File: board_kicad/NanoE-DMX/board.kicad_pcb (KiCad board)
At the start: 2 copper layers, 68.6 x 53.3 mm, 54 parts, among them J1 Conn_01x02, J20 Conn_01x02, J30 Conn_01x03, J40 RJ45, Q20 IRLM5203 (PMOS_GSD), Q21 IRLM5203 (PMOS_GSD), U1 Arduino_Nano_Every, U2 74LVC2G34, U20 TPS259630, U30 ADUM1301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

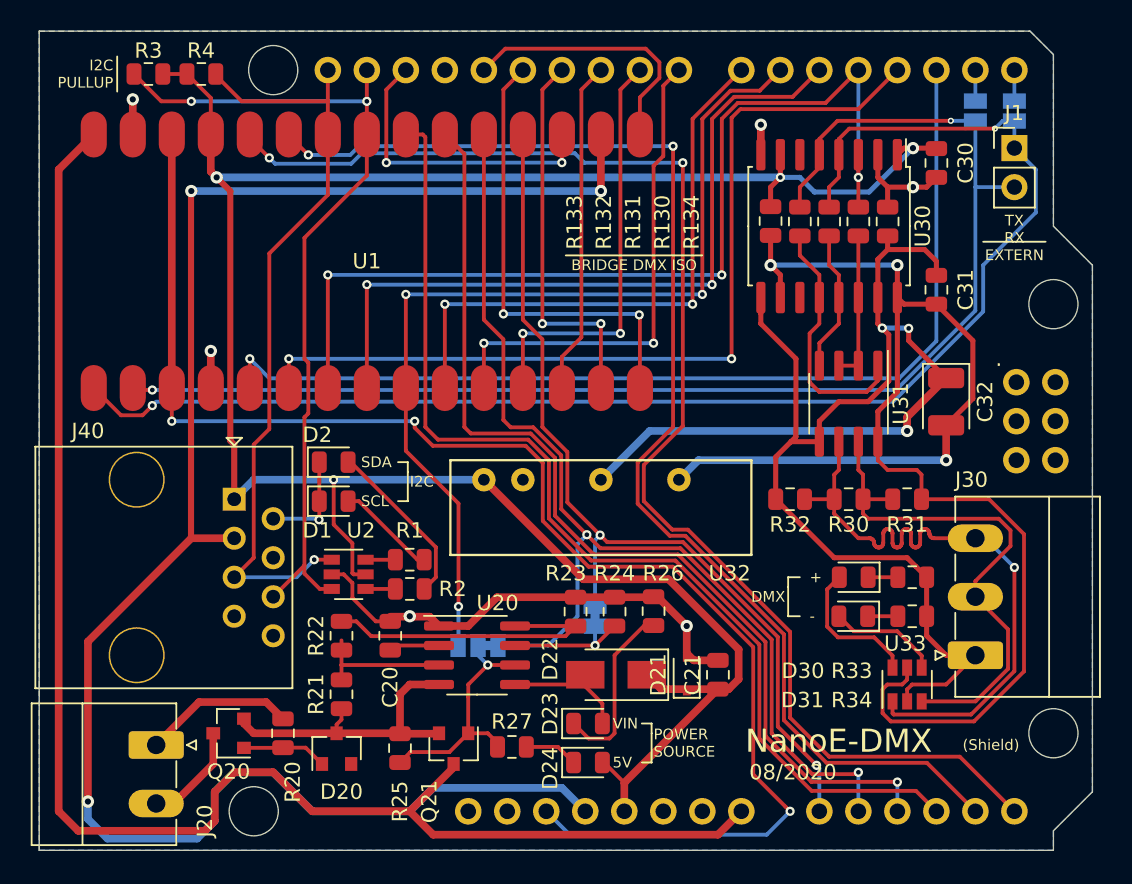
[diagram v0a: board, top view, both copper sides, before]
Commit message: added values and manufacurer id (kicost), improvements
BOTH
- added missing values for resitors and diodes
- added manf# for calculating and ordering with kicost
- minor improvements

NanoE-dmx
- bus controll LEDs (buffered) fixed for TX/RX, SDA/SCL
- changed J40 (RJ45(8pol)->Conn(4pol)
- added ISO 5V LED

UI-Shield
- Replaced U2 (MAX5026->LM2705), for higher max current
- added 2 leds at NC IO ports
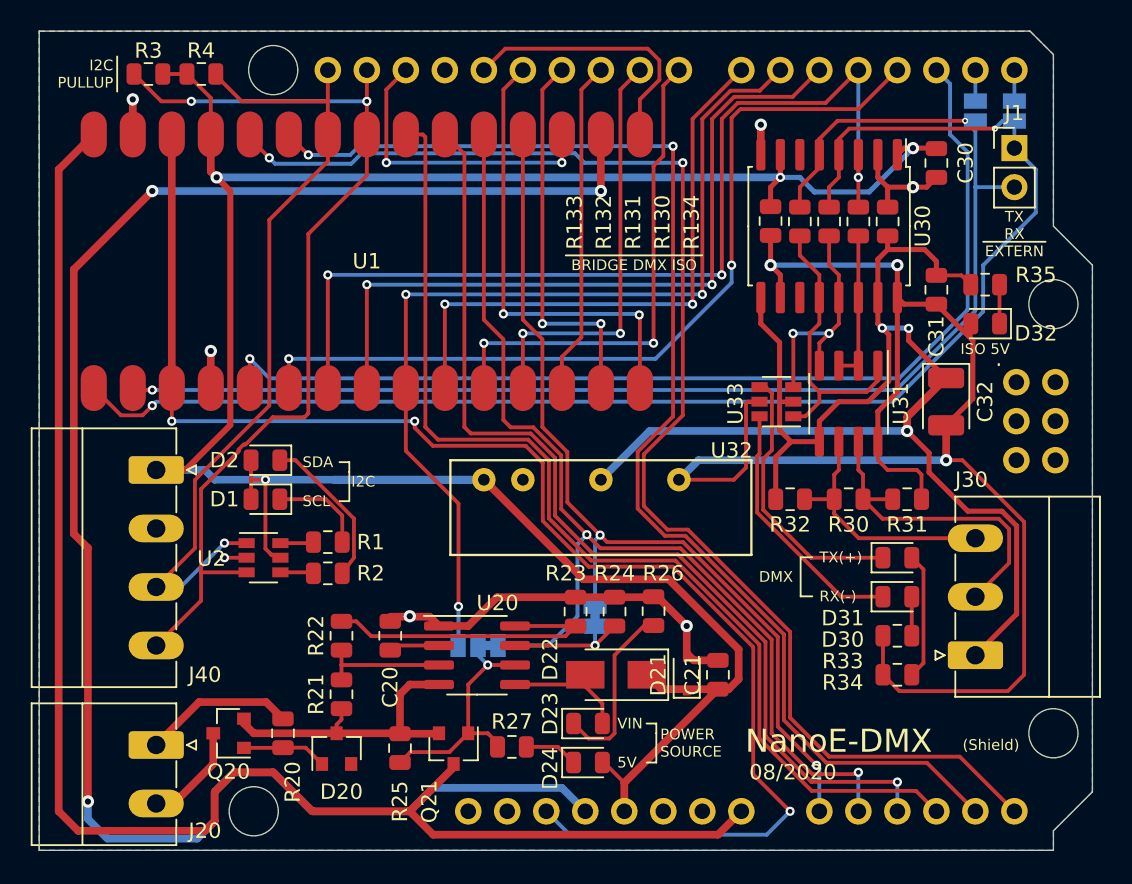
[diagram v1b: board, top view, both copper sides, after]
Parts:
- added D32: LED red, LED_SMD:LED_0805_2012Metric, F.Cu at (153.0, 95.2)
- added R35: 560, Resistor_SMD:R_0805_2012Metric, F.Cu at (153.0, 92.7)
- D1, D2, D30, D31: value LED -> LED yellow
- D23: value LED -> LED orange
- D24: value LED -> LED green
- J40: value RJ45 -> Conn_01x04; footprint Connector_RJ:RJ45_OST_PJ012-8P8CX_Vertical -> Connector_Phoenix_MC:PhoenixContact_MC_1,5_4-G-3.81_1x04_P3.81mm_Horizontal
- R1, R2, R26, R27, R33, R34: value 270 -> 560
- U32: value DCDC-SIP7-1-2-4-6 -> RFB-0505S
- moved U33 20.3 mm to (139.4, 100.3), turned to 180 degrees
- moved U2 5.65 mm to (106.0, 110.5)
- moved R1 5.46 mm to (110.2, 109.5)
- moved R2 5.43 mm to (110.2, 111.5)
- moved J40 5.43 mm to (99.1, 104.8)
- moved D31 4.77 mm to (147.3, 110.5), turned to 0 degrees
- moved D1 4.45 mm to (106.2, 106.7), turned to 180 degrees
- moved D2 4.45 mm to (106.2, 104.1), turned to 180 degrees
- moved R34 3.93 mm to (147.3, 118.1), turned to 0 degrees
- moved R33 3.93 mm to (147.3, 115.6), turned to 0 degrees
- moved D30 3.11 mm to (147.3, 113.0), turned to 0 degrees
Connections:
- D1 pad 1: GND -> Net-(D1-Pad1)
- D1 pad 2: Net-(D1-Pad2) -> +5V
- D2 pad 1: GND -> Net-(D2-Pad1)
- D2 pad 2: Net-(D2-Pad2) -> +5V
- J40 pad 3: +3V3 -> /SCL
- J40 pad 4: /IO3 -> /SDA
- R1 pad 1: Net-(D1-Pad2) -> Net-(D1-Pad1)
- R2 pad 1: Net-(D2-Pad2) -> Net-(D2-Pad1)
- R33 pad 1: /ISO_GND -> /ISO_+5V
- R33 pad 2: Net-(D30-Pad1) -> Net-(D30-Pad2)
- R34 pad 1: /ISO_GND -> /ISO_+5V
- R34 pad 2: Net-(D31-Pad1) -> Net-(D31-Pad2)
- U33 pad 1: /DMX+ -> /ISO_RX
- U33 pad 3: /DMX- -> /ISO_TX
- U33 pad 4: Net-(D31-Pad2) -> Net-(D31-Pad1)
- U33 pad 6: Net-(D30-Pad2) -> Net-(D30-Pad1)
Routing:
- net /DMX+: track 42.1 -> 17.2 mm, vias 1 -> 0
- net +5V: track 150.2 -> 167.6 mm
- net Net-(D31-Pad1): track 1.97 -> 17.9 mm
- net Net-(D30-Pad1): track 1.94 -> 16.8 mm
- net /DMX-: track 34.1 -> 21.4 mm
- net GND: track 61.2 -> 50.2 mm
- net Net-(D2-Pad2): track 10.9 -> 0.00 mm
- net Net-(D2-Pad1): track 0.00 -> 10.2 mm
- net /ISO_+5V: track 96.5 -> 105.3 mm
- net /SDA: track 55.6 -> 63.3 mm
- net Net-(D30-Pad2): track 9.36 -> 2.54 mm
- net Net-(D1-Pad2): track 6.36 -> 0.00 mm
- net Net-(D1-Pad1): track 0.00 -> 6.23 mm
- net /ISO_TX: track 9.24 -> 15.1 mm, vias 0 -> 2
- net /SCL: track 50.4 -> 53.4 mm
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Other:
- board text added: "ISO 5V"
- board text added: "RX(-)"
- board text added: "TX(+)"
- board text removed: "+"
- board text removed: "-"

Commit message: minor cleanup
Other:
- board text added: "RX"
- board text added: "TX"
- board text removed: "RX(-)"
- board text removed: "TX(+)"
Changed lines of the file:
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@@
     (effects (font (size 0.7 0.7) (thickness 0.1)) (justify right))
   )
-  (gr_line (start 141.0208 113.0046) (end 141.0208 110.49) (layer F.SilkS) (width 0.12))
-  (gr_text "RX(-)" (at 142.24 113.0046) (layer F.SilkS)
-    (effects (font (size 0.7 0.7) (thickness 0.1)) (justify left))
-  )
-  (gr_text DMX (at 138.303 111.7346) (layer F.SilkS)
-    (effects (font (size 0.7 0.7) (thickness 0.1)) (justify left))
-  )
-  (gr_line (start 141.7828 113.0046) (end 141.0208 113.0046) (layer F.SilkS) (width 0.12))
-  (gr_text "TX(+)" (at 142.24 110.4646) (layer F.SilkS)
-    (effects (font (size 0.7 0.7) (thickness 0.1)) (justify left))
-  )
-  (gr_line (start 141.7828 110.4646) (end 141.0208 110.4646) (layer F.SilkS) (width 0.12))
+  (gr_line (start 142.1003 113.0046) (end 142.1003 110.49) (layer F.SilkS) (width 0.12))
+  (gr_text RX (at 143.3195 113.0046) (layer F.SilkS)
+    (effects (font (size 0.7 0.7) (thickness 0.1)) (justify left))
+  )
+  (gr_text DMX (at 139.3825 111.7346) (layer F.SilkS)
+    (effects (font (size 0.7 0.7) (thickness 0.1)) (justify left))
+  )
+  (gr_line (start 142.8623 113.0046) (end 142.1003 113.0046) (layer F.SilkS) (width 0.12))
+  (gr_text TX (at 143.3195 110.4646) (layer F.SilkS)
+    (effects (font (size 0.7 0.7) (thickness 0.1)) (justify left))
+  )
+  (gr_line (start 142.8623 110.4646) (end 142.1003 110.4646) (layer F.SilkS) (width 0.12))
   (gr_line (start 110.998 106.807) (end 111.633 106.807) (layer F.SilkS) (width 0.12))
   (gr_line (start 110.998 104.267) (end 111.633 104.267) (layer F.SilkS) (width 0.12))
@@
   (segment (start 98.806 99.568) (end 147.236276 99.568) (width 0.25) (layer B.Cu) (net 24))
   (segment (start 154.94 86.36) (end 152.4 86.36) (width 0.25) (layer B.Cu) (net 24) (status 10))
-  (via (at 151.73201 82.042) (size 0.4) (drill 0.2) (layers F.Cu B.Cu) (net 24) (status 30))
-  (segment (start 142.24 83.225) (end 143.423 82.042) (width 0.25) (layer F.Cu) (net 24) (status 10))
-  (segment (start 152.4 86.36) (end 152.4 82.70999) (width 0.25) (layer B.Cu) (net 24))
-  (segment (start 143.423 82.042) (end 151.73201 82.042) (width 0.25) (layer F.Cu) (net 24))
-  (segment (start 152.4 82.70999) (end 151.73201 82.042) (width 0.25) (layer B.Cu) (net 24) (status 20))
-  (segment (start 142.24 84.25) (end 142.24 83.225) (width 0.25) (layer F.Cu) (net 24) (status 30))
+  (segment (start 143.423 82.042) (end 142.24 83.225) (width 0.25) (layer F.Cu) (net 24))
+  (segment (start 151.3205 82.042) (end 143.423 82.042) (width 0.25) (layer F.Cu) (net 24))
+  (segment (start 142.24 83.225) (end 142.24 84.25) (width 0.25) (layer F.Cu) (net 24))
+  (via (at 151.3205 82.042) (size 0.4) (drill 0.2) (layers F.Cu B.Cu) (net 24))
+  (segment (start 152.4 82.042) (end 152.4 86.36) (width 0.25) (layer B.Cu) (net 24))
+  (segment (start 151.3205 82.042) (end 152.4 82.042) (width 0.25) (layer B.Cu) (net 24))
   (segment (start 146.05 98.957) (end 146.05 97.982) (width 0.25) (layer F.Cu) (net 25) (status 20))
   (segment (start 141.605 99.06) (end 142.24 99.695) (width 0.25) (layer F.Cu) (net 25))

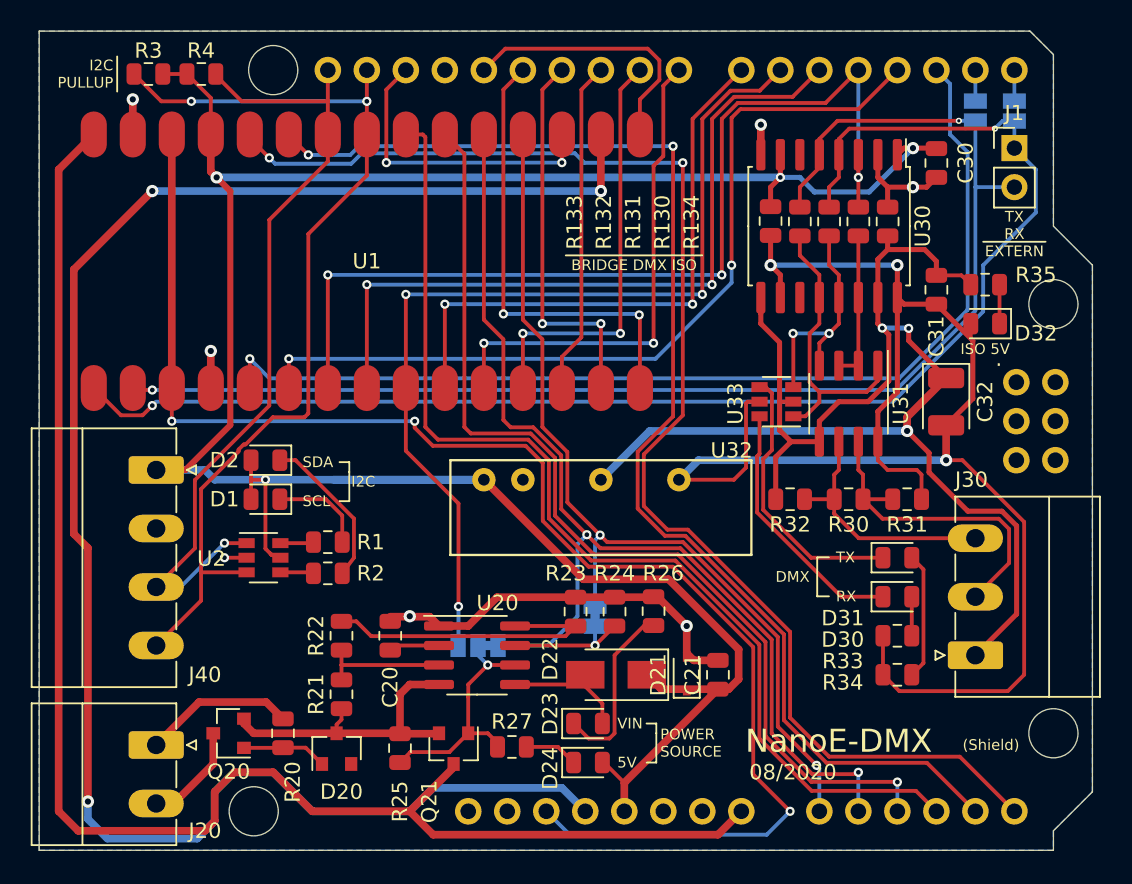
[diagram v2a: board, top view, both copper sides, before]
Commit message: fixed minor mistakes, but U1 footprint is still wrong
- silkscreen of C21 and D21
- added connector pin description
- wrong footprint (was without thermal pad) for U20
- U20 (TPS259630) footrpint association also fixed in library
- silkscreen Power Source swapped
- C32 replaced tantal with ceramic condesnator (polarity was wrong)
- changed D30, D31 (A->K, K->A) and connected resitors to ground
  (U33 is now a source) (LEDs where on on idle)

TODO (for Rev: 1): fix footprint U1 and reroute
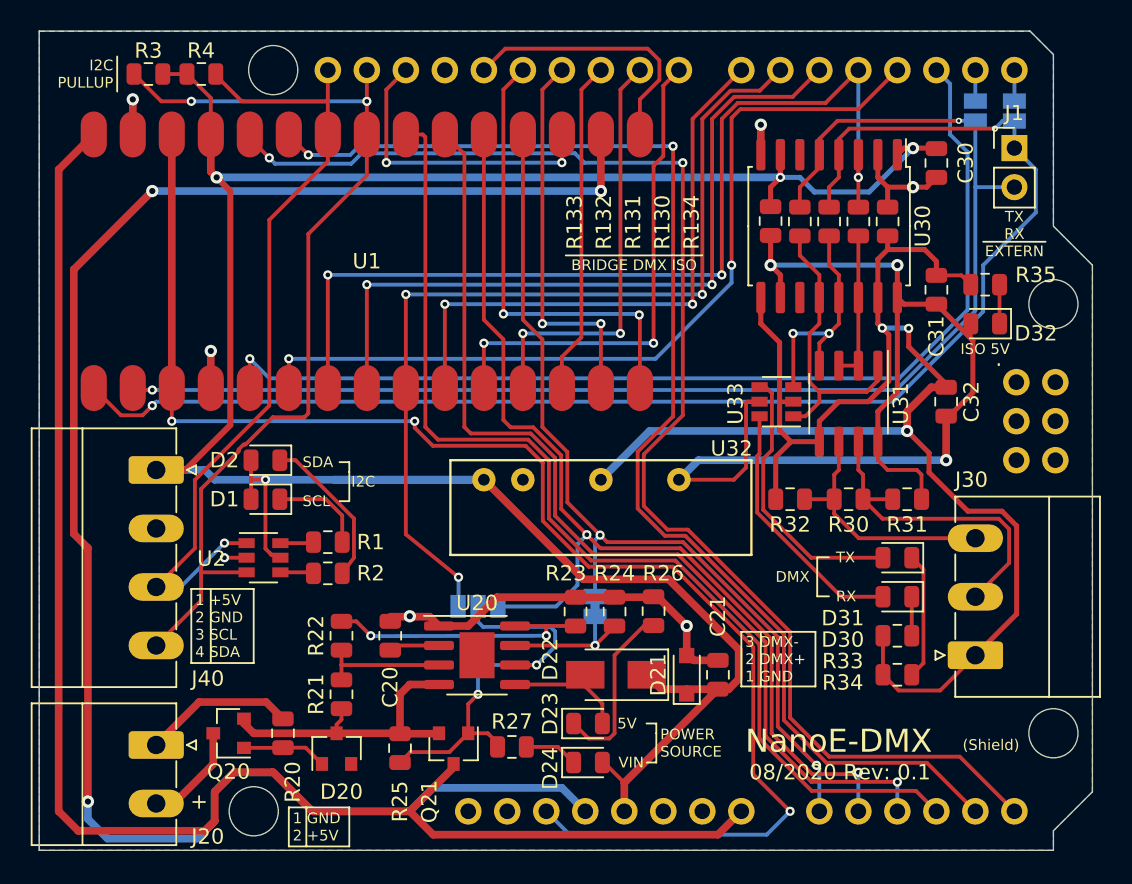
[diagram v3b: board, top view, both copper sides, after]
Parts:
- C32: footprint Capacitor_Tantalum_SMD:CP_EIA-3528-15_AVX-H -> Capacitor_SMD:C_0805_2012Metric
- D21: footprint Diode_SMD:D_SOD-323F -> Diode_SMD:D_SOD-323_HandSoldering
- R1, R2, R26, R27, R33, R34, R35: value 560 -> 1k
- R3, R4: value R -> 10k
- U20: footprint Package_SO:SOIC-8_3.9x4.9mm_P1.27mm -> Package_SO:SOIC-8-1EP_3.9x4.9mm_P1.27mm_EP2.29x3mm
- moved JP4 2.54 mm to (120.0, 113.7)
- moved JP3 0.63 mm to (127.6, 113.7)
- turned D30 to 180 degrees
- turned D31 to 180 degrees
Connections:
- R33 pad 1: /ISO_+5V -> /ISO_GND
- R33 pad 2: Net-(D30-Pad2) -> Net-(D30-Pad1)
- R34 pad 1: /ISO_+5V -> /ISO_GND
- R34 pad 2: Net-(D31-Pad2) -> Net-(D31-Pad1)
- U33 pad 4: Net-(D31-Pad1) -> Net-(D31-Pad2)
- U33 pad 6: Net-(D30-Pad1) -> Net-(D30-Pad2)
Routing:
- net /ISO_+5V: track 105.3 -> 76.1 mm
- net Net-(D30-Pad2): track 2.54 -> 16.8 mm
- net Net-(D30-Pad1): track 16.8 -> 2.54 mm
- net /~FLT: track 15.9 -> 26.5 mm, vias 1 -> 2
- net /ISO_GND: track 93.7 -> 104.2 mm
- net Net-(D31-Pad2): track 8.25 -> 17.9 mm
- net Net-(D31-Pad1): track 17.9 -> 8.25 mm
- net /D6-~FLT: track 61.4 -> 59.1 mm
- net /A1-~FLT: track 71.5 -> 69.3 mm
- net Net-(R22-Pad2): track 19.9 -> 18.3 mm, vias 0 -> 2
- net /CUR: track 8.26 -> 8.91 mm
- net /A0-CUR: track 60.5 -> 59.9 mm
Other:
- board text added: "+"
- board text added: "08/2020 Rev: 0.1"
- board text added: "1 +5V 2 GND 3 SCL 4 SDA"
- board text added: "1 GND 2 +5V"
- board text added: "3 DMX- 2 DMX+ 1 GND"
- board text removed: "08/2020"

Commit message: fixed errors in NanoE-DMX and UI-Shield
NanoE-DMX -> Rev: 1.0:
- see previous commit
- fixed footprint of U1
- reroutet corresponding tracks
- added ICSP header to board

UI-Shield -> Rev: 1.0:
- added ICSP header to board
- optional (exclusive) I2C for OLED and IO-Expander
- selectable SPI source (ICSP/D12-D10)
- fixed LCD SPI interchanged communication lines
- added dimming for LED-Buttons and LEDs
- fixed erros in OLED routing
	- I2C only tested on plugboard
	- SPI not testet
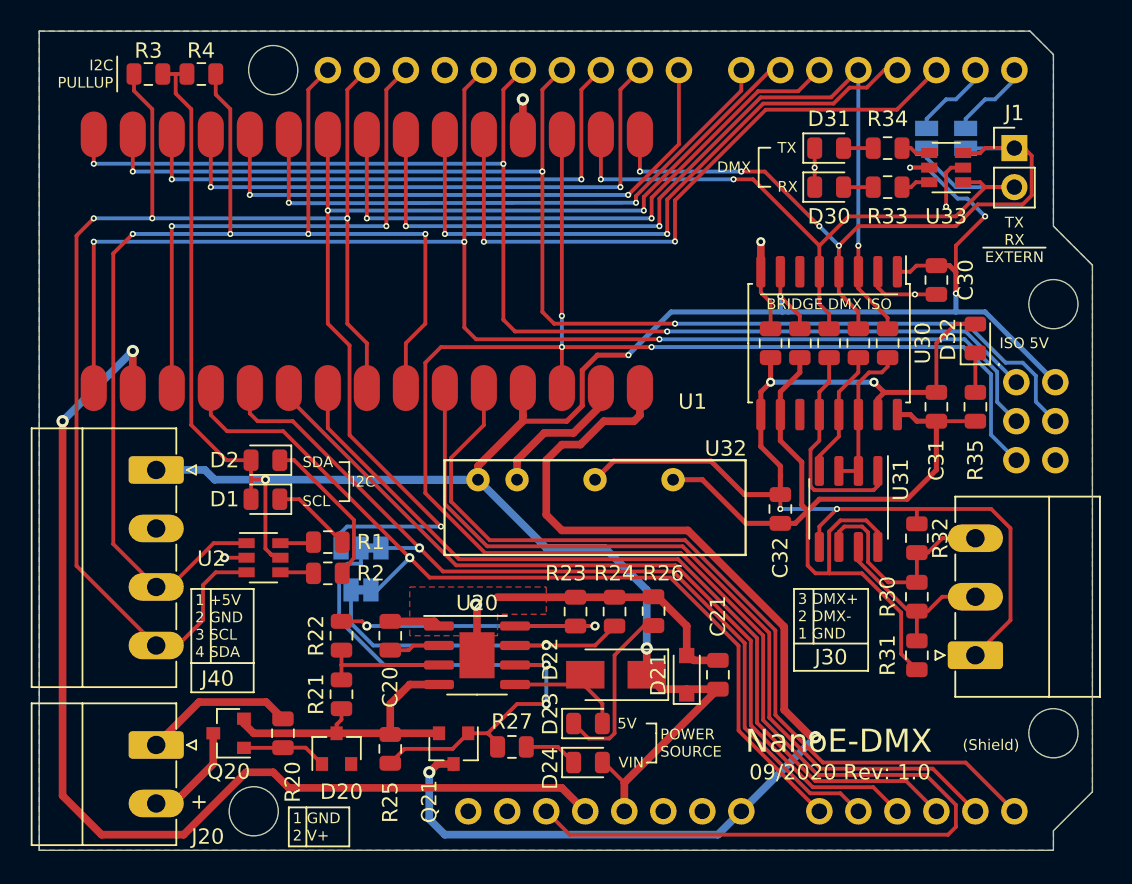
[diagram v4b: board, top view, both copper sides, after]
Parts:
- moved R34 34.3 mm to (146.7, 83.8)
- moved R33 29.2 mm to (146.7, 86.4)
- moved D30 27.0 mm to (142.9, 86.4), turned to 0 degrees
- moved D31 27.0 mm to (142.9, 83.8), turned to 0 degrees
- moved U33 18.8 mm to (150.5, 85.1)
- moved JP3 15.3 mm to (112.4, 112.6), turned to 0 degrees
- moved C32 12.9 mm to (139.7, 107.3)
- moved R134 11.0 mm to (139.1, 96.5)
- moved R31 10.2 mm to (148.6, 116.8), turned to 90 degrees
- moved R32 8.64 mm to (148.6, 109.2), turned to 90 degrees
- moved JP4 8.52 mm to (112.4, 109.9)
- moved R133 8.18 mm to (141.0, 96.5)
- moved R130 8.15 mm to (146.7, 96.5)
- moved R131 8.15 mm to (144.8, 96.5)
- moved R132 8.15 mm to (142.9, 96.5)
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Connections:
- D30 pad 1: Net-(D30-Pad1) -> GND
- D31 pad 1: Net-(D31-Pad1) -> GND
- D32 pad 2: /ISO_+5V -> /ISO_GND
- R33 pad 1: /ISO_GND -> Net-(D30-Pad2)
- R33 pad 2: Net-(D30-Pad1) -> Net-(R33-Pad2)
- R34 pad 1: /ISO_GND -> Net-(D31-Pad2)
- R34 pad 2: Net-(D31-Pad1) -> Net-(R34-Pad2)
- R35 pad 1: Net-(D32-Pad1) -> /ISO_+5V
- R35 pad 2: /ISO_GND -> Net-(D32-Pad1)
- U20 pad 9: (no net) -> GND
- U33 pad 1: /ISO_RX -> /RX
- U33 pad 2: /ISO_GND -> GND
- U33 pad 3: /ISO_TX -> /TX
- U33 pad 4: Net-(D31-Pad2) -> Net-(R34-Pad2)
- U33 pad 5: /ISO_+5V -> +5V
- U33 pad 6: Net-(D30-Pad2) -> Net-(R33-Pad2)
- XA1 pad 5V2: Net-(XA1-Pad5V2) -> +5V
- XA1 pad GND4: Net-(XA1-PadGND4) -> GND
- XA1 pad MISO: Net-(XA1-PadMISO) -> /MISO
- XA1 pad MOSI: Net-(XA1-PadMOSI) -> /MOSI
- XA1 pad RST2: Net-(XA1-PadRST2) -> /~RESET
- XA1 pad SCK: Net-(XA1-PadSCK) -> /SCK
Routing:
- net /SCK: track 17.7 -> 90.6 mm, vias 0 -> 3
- net /MOSI: track 25.0 -> 82.7 mm, vias 2 -> 3
- net /~RESET: track 93.9 -> 144.4 mm
- net /MISO: track 30.1 -> 80.4 mm, vias 2 -> 3
- net /TX: track 92.5 -> 47.8 mm, vias 2 -> 4
- net +3V3: track 114.4 -> 71.1 mm, vias 3 -> 2
- net /RX: track 87.7 -> 48.4 mm
- net /ISO_GND: track 104.2 -> 71.7 mm, vias 3 -> 4
- net /A5: track 88.7 -> 56.5 mm, vias 2 -> 0
- net /SCL: track 53.4 -> 84.9 mm, vias 1 -> 4
- net /A4: track 83.8 -> 53.6 mm, vias 2 -> 0
- net /VIN: track 99.3 -> 72.6 mm, vias 0 -> 2
- net /D2: track 67.5 -> 42.6 mm, vias 1 -> 2
- net /SDA: track 63.3 -> 87.8 mm, vias 2 -> 3
- net Net-(D31-Pad2): track 17.9 -> 1.94 mm
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- added copper zone on F.Cu, net GND
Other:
- net class deault add clearance removed
- net class pwr: via_dia 0.8 -> 0.6; via_drill 0.4 -> 0.3
- board text added: "09/2020 Rev: 1.0"
- board text added: "1 GND 2 V+"
- board text added: "3 DMX+ 2 DMX- 1 GND"
- board text added: "5V 5V"
- board text added: "BBQ BBQ"
- board text added: "Power Input 0.0V < 4.7V < 5.5V < 21.0V"
- board text added: "Q21"
- board text added: "UART"
- board text added: "UVLO UVLO"
- board text added: "VIN OVLO"
- board text added: "reverse polarity protection up to 30V"
- board text removed: "08/2020 Rev: 0.1"
- board text removed: "1 GND 2 +5V"
- board text removed: "3 DMX- 2 DMX+ 1 GND"
